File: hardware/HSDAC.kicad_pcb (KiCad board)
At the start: 2 copper layers, 70 x 24.6 mm, 75 parts, among them IC1 ES9018K2M, J1 SM07B-SRSS-TB__LF__SN_, J3 USB_C_Receptacle_USB2.0_16P, SW1 RST, U1 CH32V305FBP6, U2 ME6210A33M3G, U3 OPA1678, U4 OPA1678, U5 OPA1678, X1 8M

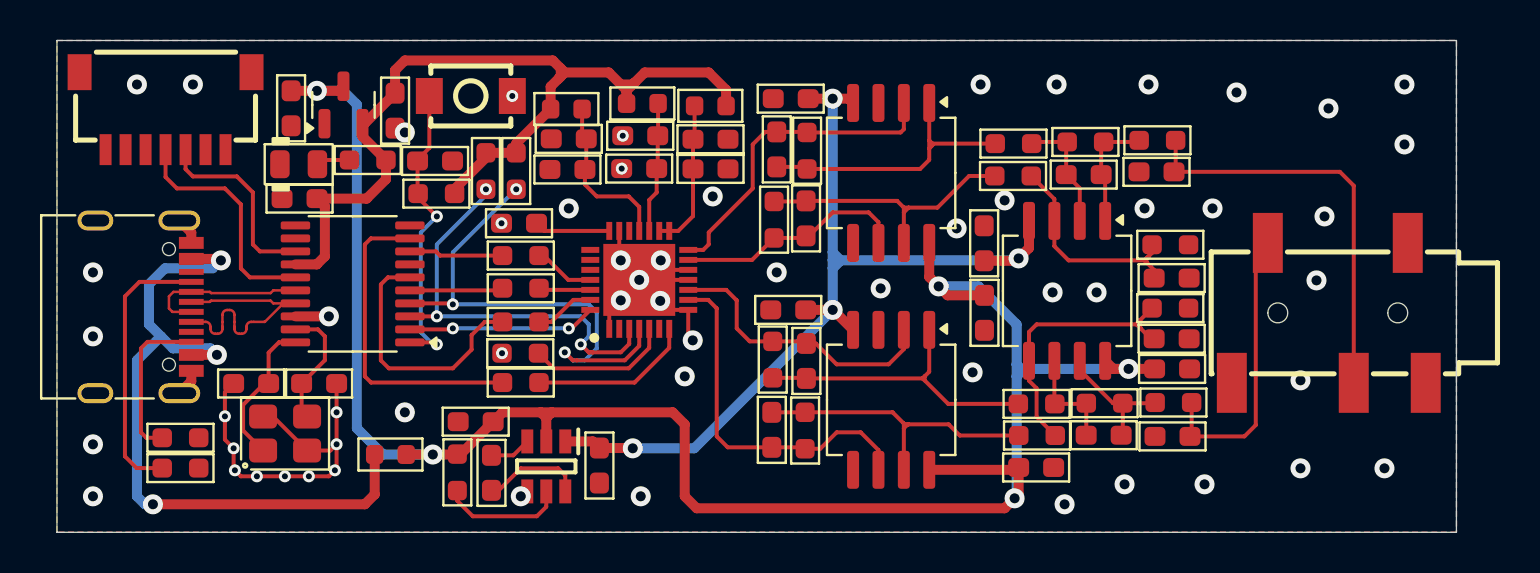
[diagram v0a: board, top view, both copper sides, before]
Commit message: 修复声道和运放封装错误
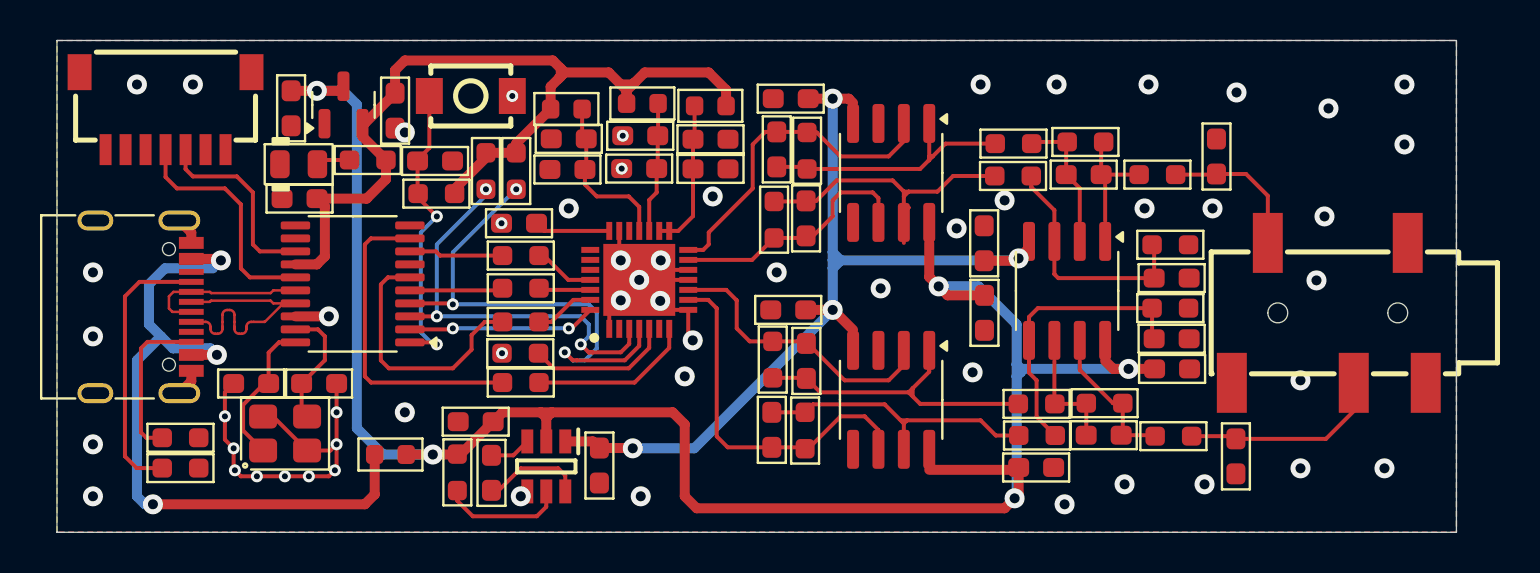
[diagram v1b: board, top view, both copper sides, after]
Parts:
- C26, C27: value 4.7nF -> 100nF
- R24, R25: value 40 -> 51
- U3, U4, U5: footprint Package_SO:SOIC-8_5.3x6.2mm_P1.27mm -> Package_SO:SOIC-8_3.9x4.9mm_P1.27mm
- moved R24 14.8 mm to (139.6, 36.8)
- moved C26 14.8 mm to (142.8, 37.8), turned to 90 degrees
- moved C27 14.2 mm to (141.8, 22.8), turned to -90 degrees
- moved R25 11.4 mm to (138.8, 23.7)
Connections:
- R24 pad 2: Net-(C22-Pad2) -> Net-(C24-Pad2)
- R25 pad 2: Net-(C24-Pad2) -> Net-(C22-Pad2)
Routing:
- net Net-(C26-Pad2): track 20.8 -> 10.2 mm
- net Net-(C27-Pad2): track 14.6 -> 7.43 mm
- net Net-(C18-Pad2): track 14.0 -> 16.3 mm
- net -5V: track 46.4 -> 45.0 mm
- net Net-(U5A-+): track 11.2 -> 12.2 mm
- net /DACL: track 11.7 -> 12.7 mm
- net Net-(C17-Pad2): track 14.4 -> 13.5 mm
- net Net-(C20-Pad2): track 15.5 -> 14.9 mm
- net GND: vias 58 -> 56
